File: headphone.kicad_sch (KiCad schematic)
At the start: 5 parts, among them P1 FPC0.5MM14PPulltypeH2.0mmPick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, Q4 TPNTK3139PT1G

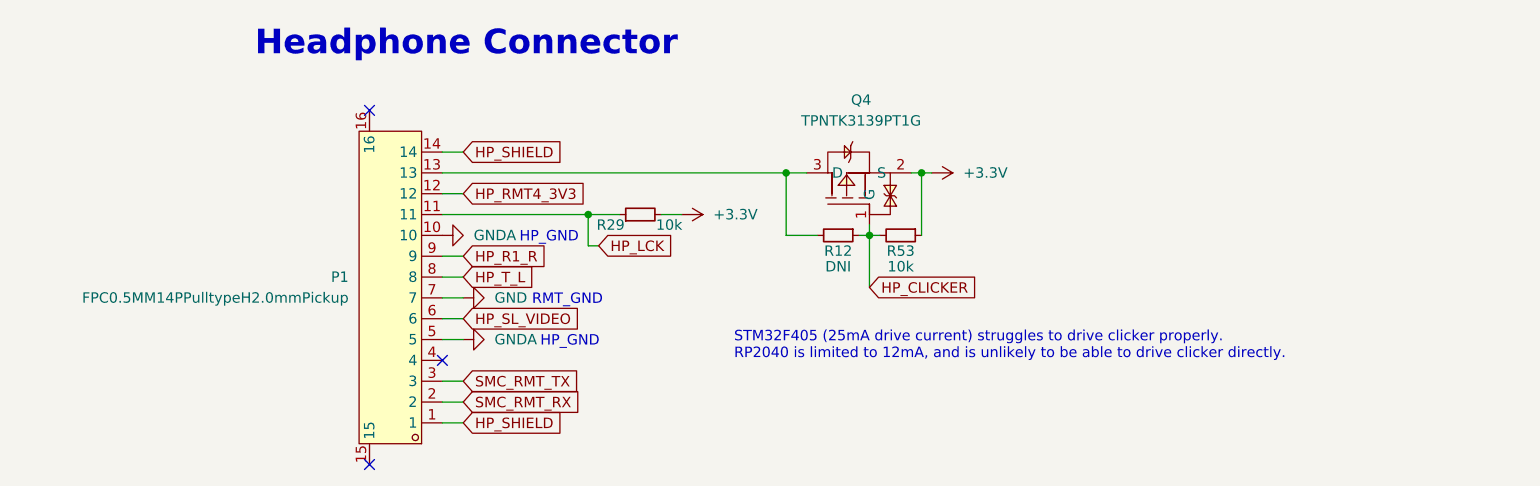
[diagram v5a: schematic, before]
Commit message: schem: migrate away from LCSC exclusive parts
- layout: migrate away from lcsc footprints
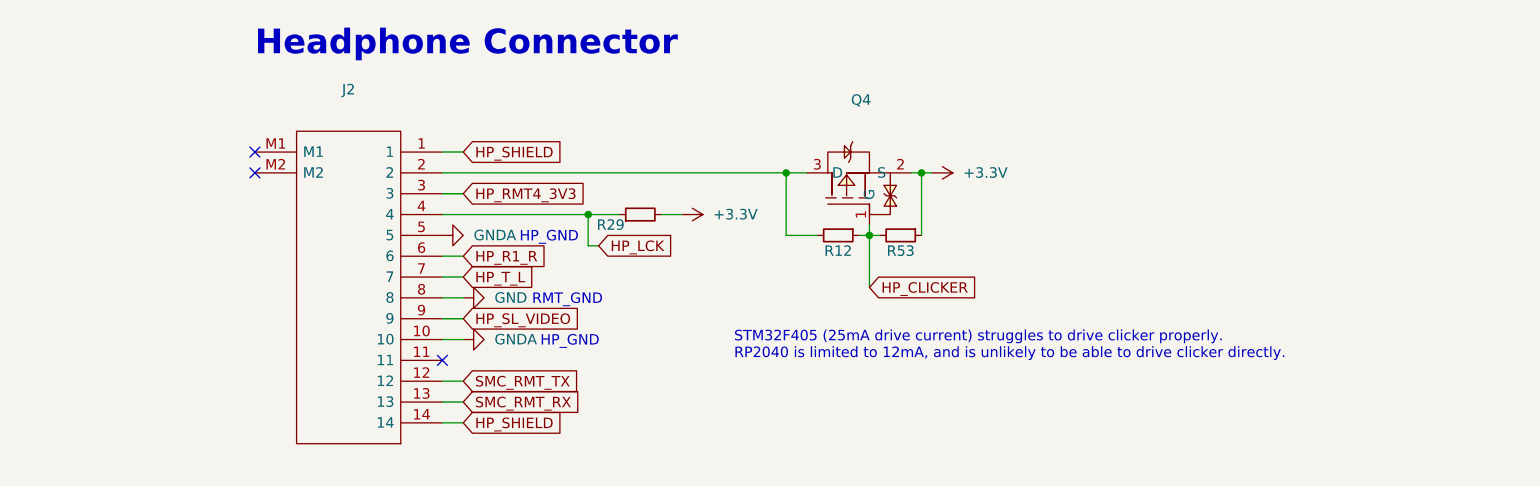
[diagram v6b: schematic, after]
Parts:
- removed P1: FPC0.5MM14PPulltypeH2.0mmPickup, lcsc:FPC-SMD_14P-L12.5-W5.4-P0.50, symbol lcsc:FPC0.5MM14PPulltypeH2.0mmPickup
- added J2: (no value), symbol gigahawk:SFV14R-2STE1HLF
- Q4: value TPNTK3139PT1G -> (none); footprint lcsc:SOT-723_L1.2-W0.8-P0.40-LS1.2-BR -> (none); Manufacturer Part (none) -> TPNTK3139PT1G
- R12: value DNI -> (none); footprint Resistor_SMD:R_0402_1005Metric -> (none)
- R29, R53: value 10k -> (none); footprint Resistor_SMD:R_0402_1005Metric -> (none)
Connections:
- net GND: now also J2.8
- net GNDA: now also J2.10, J2.5
- net HP_LCK: now also J2.4
- net HP_R1_R: now also J2.6
- net HP_RMT4_3V3: now also J2.3
- net HP_SHIELD: now also J2.1, J2.14
- net HP_SL_VIDEO: now also J2.9
- net HP_T_L: now also J2.7
- net SMC_RMT_RX: now also J2.13
- net SMC_RMT_TX: now also J2.12
- net at Q4.3 (D), R12.2: now also J2.2

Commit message: layout: update footprint for TP4056M
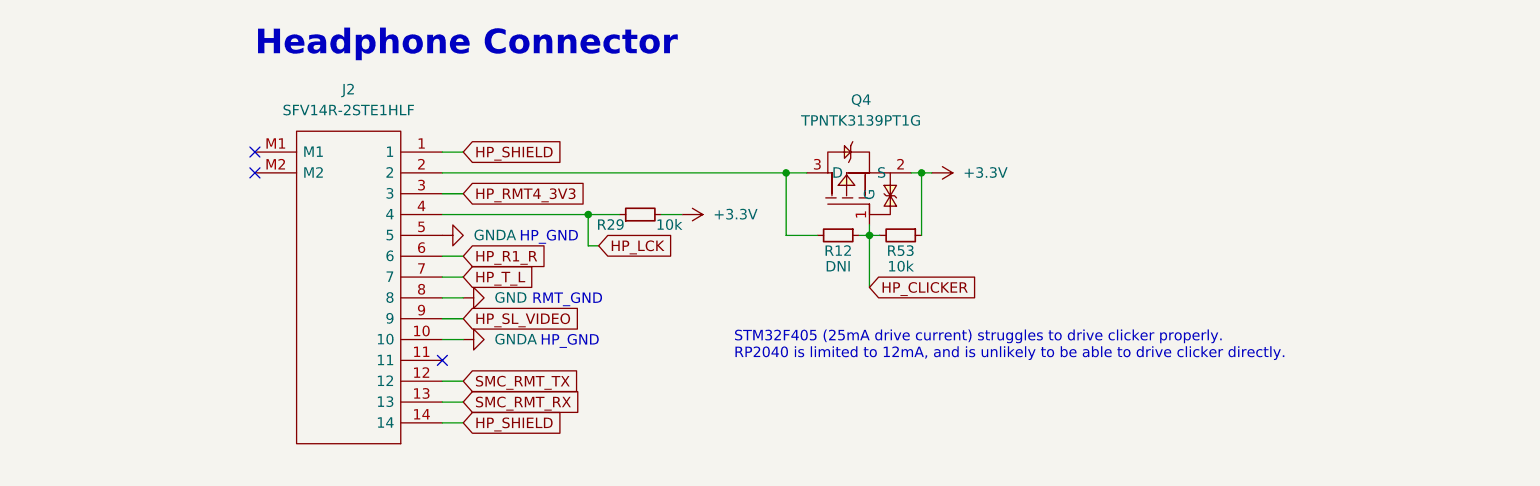
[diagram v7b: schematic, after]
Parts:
- J2: value (none) -> SFV14R-2STE1HLF; footprint (none) -> Gigahawk:SFV14R2STE1HLF
- Q4: value (none) -> TPNTK3139PT1G; footprint (none) -> Package_TO_SOT_SMD:SOT-723
- R12: value (none) -> DNI; footprint (none) -> Resistor_SMD:R_0402_1005Metric
- R29, R53: value (none) -> 10k; footprint (none) -> Resistor_SMD:R_0402_1005Metric
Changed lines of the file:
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@@
     (in_bom yes) (on_board yes) (fields_autoplaced)
     (property "Reference" "Q4" (id 0) (at 181.865 95.25 90))
-    (property "Value" "" (id 1) (at 181.865 97.79 90))
-    (property "Footprint" "" (id 2) (at 193.04 104.14 0)
+    (property "Value" "TPNTK3139PT1G" (id 1) (at 181.865 97.79 90))
+    (property "Footprint" "Package_TO_SOT_SMD:SOT-723" (id 2) (at 193.04 104.14 0)
       (effects (font (size 1.27 1.27)) hide)
     )
@@
     (in_bom yes) (on_board yes)
     (property "Reference" "R53" (id 0) (at 186.69 113.665 90))
-    (property "Value" "" (id 1) (at 186.69 115.57 90))
-    (property "Footprint" "" (id 2) (at 186.69 111.76 0)
+    (property "Value" "10k" (id 1) (at 186.69 115.57 90))
+    (property "Footprint" "Resistor_SMD:R_0402_1005Metric" (id 2) (at 186.69 111.76 0)
       (effects (font (size 1.27 1.27)) hide)
     )
@@
     (in_bom yes) (on_board yes) (fields_autoplaced)
     (property "Reference" "J2" (id 0) (at 119.38 93.98 0))
-    (property "Value" "" (id 1) (at 119.38 96.52 0))
-    (property "Footprint" "" (id 2) (at 127 99.06 0)
+    (property "Value" "SFV14R-2STE1HLF" (id 1) (at 119.38 96.52 0))
+    (property "Footprint" "Gigahawk:SFV14R2STE1HLF" (id 2) (at 127 99.06 0)
       (effects (font (size 1.27 1.27)) (justify left) hide)
     )
@@
     (in_bom yes) (on_board yes)
     (property "Reference" "R12" (id 0) (at 179.07 113.665 90))
-    (property "Value" "" (id 1) (at 179.07 115.57 90))
-    (property "Footprint" "" (id 2) (at 179.07 111.76 0)
+    (property "Value" "DNI" (id 1) (at 179.07 115.57 90))
+    (property "Footprint" "Resistor_SMD:R_0402_1005Metric" (id 2) (at 179.07 111.76 0)
       (effects (font (size 1.27 1.27)) hide)
     )
@@
       (effects (font (size 1.27 1.27)) (justify left))
     )
-    (property "Value" "" (id 1) (at 156.845 110.49 90)
+    (property "Value" "10k" (id 1) (at 156.845 110.49 90)
       (effects (font (size 1.27 1.27)) (justify right))
     )
-    (property "Footprint" "" (id 2) (at 154.94 109.22 0)
+    (property "Footprint" "Resistor_SMD:R_0402_1005Metric" (id 2) (at 154.94 109.22 0)
       (effects (font (size 1.27 1.27)) hide)
     )

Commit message: layout: preliminary layout of most of board
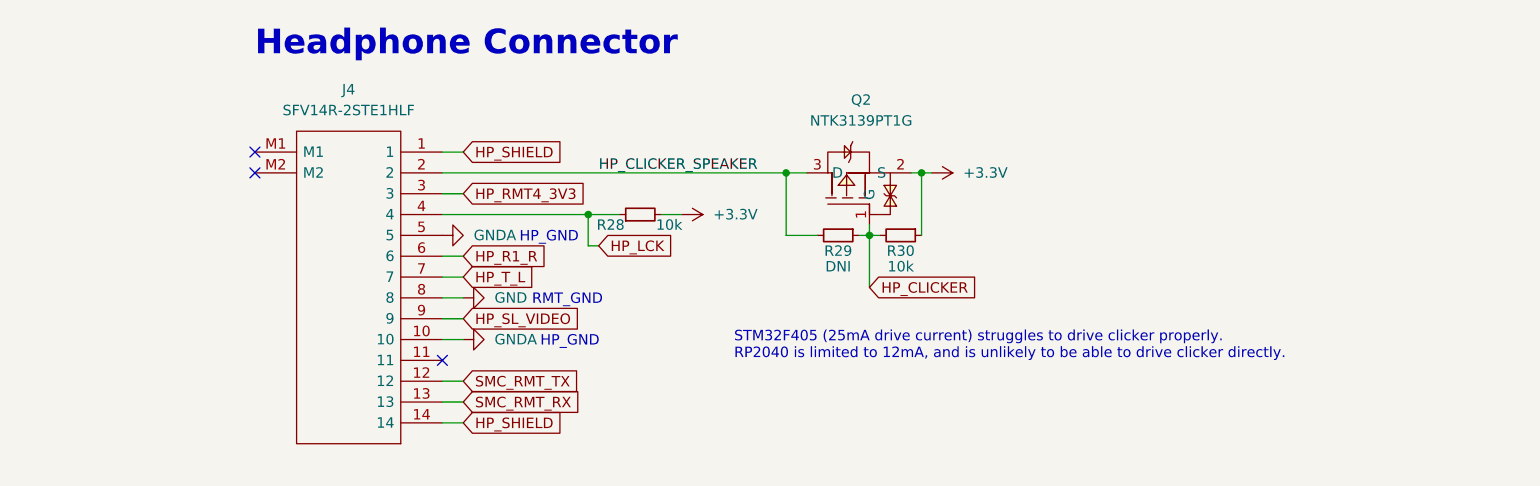
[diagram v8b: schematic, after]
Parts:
- Q2: renamed from Q4; value TPNTK3139PT1G -> NTK3139PT1G; symbol lcsc:TPNTK3139PT1G -> gigahawk:NTK3139PT1G; Digikey Part (none) -> NTK3139PT1GOSTR-ND; Digikey Price/Stock (none) -> https://www.digikey.ca/en/products/detail/onsemi/NTK3139PT1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; LCSC Part C558623 -> C236246; Manufacturer TECH PUBLIC -> onsemi; Manufacturer Part TPNTK3139PT1G -> NTK3139PT1G; Mouser Part (none) -> 863-NTK3139PT1G; Mouser Price/Stock (none) -> https://www.mouser.ca/ProductDetail/onsemi/NTK3139PT1G?qs=g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
- renumbered J2 to J4, R29 to R28, R12 to R29, R53 to R30
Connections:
- net HP_CLICKER_SPEAKER: now reaches J4.2, Q2.3 (D), R29.2
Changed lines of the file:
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@@
     (effects (font (size 1.27 1.27)) (justify left bottom))
   )
+  (label "HP_CLICKER_SPEAKER" (at 149.86 104.14 0)
+    (effects (font (size 1.27 1.27)) (justify left bottom))
+  )
   (global_label "HP_SHIELD" (shape input) (at 133.35 101.6 0) (fields_autoplaced)
     (effects (font (size 1.27 1.27)) (justify left))
@@
     )
   )
-  (symbol (lib_id "lcsc:TPNTK3139PT1G") (at 180.34 104.14 90) (unit 1)
-    (in_bom yes) (on_board yes) (fields_autoplaced)
-    (property "Reference" "Q4" (id 0) (at 181.865 95.25 90))
-    (property "Value" "TPNTK3139PT1G" (id 1) (at 181.865 97.79 90))
+  (symbol (lib_id "gigahawk:NTK3139PT1G") (at 180.34 104.14 90) (unit 1)
+    (in_bom yes) (on_board yes) (fields_autoplaced)
+    (property "Reference" "Q2" (id 0) (at 181.865 95.25 90))
+    (property "Value" "NTK3139PT1G" (id 1) (at 181.865 97.79 90))
     (property "Footprint" "Package_TO_SOT_SMD:SOT-723" (id 2) (at 193.04 104.14 0)
       (effects (font (size 1.27 1.27)) hide)
     )
-    (property "Datasheet" "https://lcsc.com/product-detail/MOSFET_TECH-PUBLIC-TPNTK3139PT1G_C558623.html" (id 3) (at 195.58 104.14 0)
-      (effects (font (size 1.27 1.27)) hide)
-    )
-    (property "Manufacturer" "TECH PUBLIC" (id 4) (at 198.12 104.14 0)
-      (effects (font (size 1.27 1.27)) hide)
-    )
-    (property "LCSC Part" "C558623" (id 5) (at 200.66 104.14 0)
+    (property "Datasheet" "https://www.onsemi.com/pdf/datasheet/ntk3139p-d.pdf" (id 3) (at 195.58 104.14 0)
+      (effects (font (size 1.27 1.27)) hide)
+    )
+    (property "Manufacturer" "onsemi" (id 4) (at 198.12 104.14 0)
+      (effects (font (size 1.27 1.27)) hide)
+    )
+    (property "LCSC Part" "C236246" (id 5) (at 200.66 104.14 0)
       (effects (font (size 1.27 1.27)) hide)
     )
@@
       (effects (font (size 1.27 1.27)) hide)
     )
-    (property "Description" "20V 850mA 530mΩ@4.5V,550mA 690mW 750mV@250uA 4.4pF@10V P Channel 58pF@10V 530pC@2.5V +150℃@(Tj) SOT-723 MOSFETs ROHS" (id 7) (at 180.34 104.14 0)
-      (effects (font (size 1.27 1.27)) hide)
-    )
-    (property "Manufacturer Part" "TPNTK3139PT1G" (id 8) (at 180.34 104.14 0)
+    (property "Description" "P-Channel 20 V 660mA (Ta) 310mW (Ta) Surface Mount SOT-723" (id 7) (at 180.34 104.14 0)
+      (effects (font (size 1.27 1.27)) hide)
+    )
+    (property "Manufacturer Part" "NTK3139PT1G" (id 8) (at 180.34 104.14 0)
+      (effects (font (size 1.27 1.27)) hide)
+    )
+    (property "Digikey Part" "NTK3139PT1GOSTR-ND" (id 9) (at 180.34 104.14 0)
+      (effects (font (size 1.27 1.27)) hide)
+    )
+    (property "Digikey Price/Stock" "https://www.digikey.ca/en/products/detail/onsemi/NTK3139PT1G/1793013" (id 10) (at 180.34 104.14 0)
+      (effects (font (size 1.27 1.27)) hide)
+    )
+    (property "Mouser Part" "863-NTK3139PT1G" (id 11) (at 180.34 104.14 0)
+      (effects (font (size 1.27 1.27)) hide)
+    )
+    (property "Mouser Price/Stock" "https://www.mouser.ca/ProductDetail/onsemi/NTK3139PT1G?qs=g97OBWmz8%2FUOleSHsosIkQ%3D%3D" (id 12) (at 180.34 104.14 0)
       (effects (font (size 1.27 1.27)) hide)
     )
@@
   (symbol (lib_id "power:GNDA") (at 133.35 124.46 90) (unit 1)
     (in_bom yes) (on_board yes) (fields_autoplaced)
-    (property "Reference" "#PWR067" (id 0) (at 139.7 124.46 0)
+    (property "Reference" "#PWR071" (id 0) (at 139.7 124.46 0)
       (effects (font (size 1.27 1.27)) hide)
     )
@@
   (symbol (lib_id "Device:R_Small") (at 186.69 111.76 270) (unit 1)
     (in_bom yes) (on_board yes)
-    (property "Reference" "R53" (id 0) (at 186.69 113.665 90))
+    (property "Reference" "R30" (id 0) (at 186.69 113.665 90))
     (property "Value" "10k" (id 1) (at 186.69 115.57 90))
     (property "Footprint" "Resistor_SMD:R_0402_1005Metric" (id 2) (at 186.69 111.76 0)
@@
   (symbol (lib_id "power:+3.3V") (at 160.02 109.22 270) (unit 1)
     (in_bom yes) (on_board yes) (fields_autoplaced)
-    (property "Reference" "#PWR068" (id 0) (at 156.21 109.22 0)
+    (property "Reference" "#PWR072" (id 0) (at 156.21 109.22 0)
       (effects (font (size 1.27 1.27)) hide)
     )
@@
   (symbol (lib_id "power:GND") (at 133.35 119.38 90) (unit 1)
     (in_bom yes) (on_board yes) (fields_autoplaced)
-    (property "Reference" "#PWR066" (id 0) (at 139.7 119.38 0)
+    (property "Reference" "#PWR070" (id 0) (at 139.7 119.38 0)
       (effects (font (size 1.27 1.27)) hide)
     )
@@
   (symbol (lib_id "power:GNDA") (at 130.81 111.76 90) (unit 1)
     (in_bom yes) (on_board yes) (fields_autoplaced)
-    (property "Reference" "#PWR0127" (id 0) (at 137.16 111.76 0)
+    (property "Reference" "#PWR069" (id 0) (at 137.16 111.76 0)
       (effects (font (size 1.27 1.27)) hide)
     )
@@
   (symbol (lib_id "power:+3.3V") (at 190.5 104.14 270) (unit 1)
     (in_bom yes) (on_board yes) (fields_autoplaced)
-    (property "Reference" "#PWR0126" (id 0) (at 186.69 104.14 0)
+    (property "Reference" "#PWR073" (id 0) (at 186.69 104.14 0)
       (effects (font (size 1.27 1.27)) hide)
     )
@@
   (symbol (lib_id "gigahawk:SFV14R-2STE1HLF") (at 107.95 101.6 0) (unit 1)
     (in_bom yes) (on_board yes) (fields_autoplaced)
-    (property "Reference" "J2" (id 0) (at 119.38 93.98 0))
+    (property "Reference" "J4" (id 0) (at 119.38 93.98 0))
     (property "Value" "SFV14R-2STE1HLF" (id 1) (at 119.38 96.52 0))
     (property "Footprint" "Gigahawk:SFV14R2STE1HLF" (id 2) (at 127 99.06 0)
@@
   (symbol (lib_id "Device:R_Small") (at 179.07 111.76 270) (unit 1)
     (in_bom yes) (on_board yes)
-    (property "Reference" "R12" (id 0) (at 179.07 113.665 90))
+    (property "Reference" "R29" (id 0) (at 179.07 113.665 90))
     (property "Value" "DNI" (id 1) (at 179.07 115.57 90))
     (property "Footprint" "Resistor_SMD:R_0402_1005Metric" (id 2) (at 179.07 111.76 0)
@@
   (symbol (lib_id "Device:R_Small") (at 154.94 109.22 90) (unit 1)
     (in_bom yes) (on_board yes)
-    (property "Reference" "R29" (id 0) (at 153.035 110.49 90)
+    (property "Reference" "R28" (id 0) (at 153.035 110.49 90)
       (effects (font (size 1.27 1.27)) (justify left))
     )
